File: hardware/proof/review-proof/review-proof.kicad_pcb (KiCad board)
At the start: 4 copper layers, 92 x 60 mm, 31 parts, among them J1 MAINS, J2 5V_IN, J4 LOAD, U1 VO3526, U2 AMS1117-3.3, U3 MCP6001-OT, U4 ATtiny85-20M, Y1 8MHz

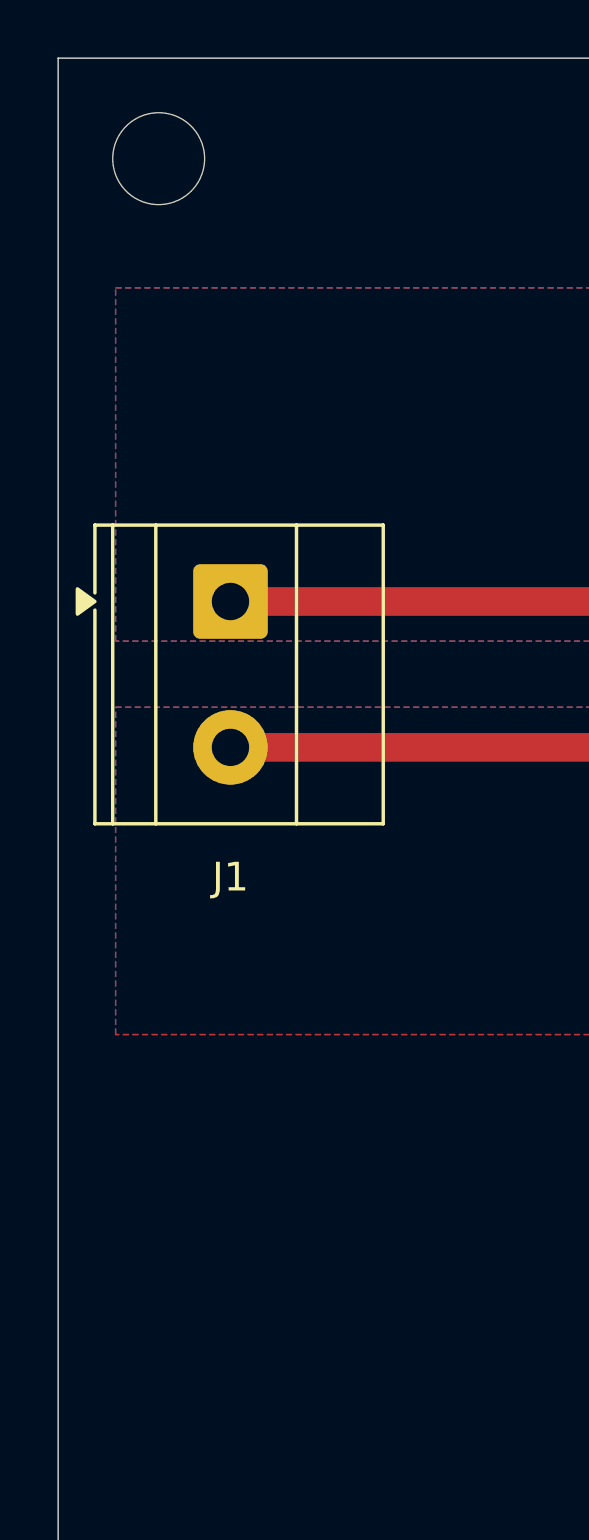
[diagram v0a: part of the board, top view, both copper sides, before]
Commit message: fix(hardware): move the review proof's mounting hole H1 clear of the mains copper the hole rule measures [SOL-PRE-ORDER-CHECK-SEPARATION-FLOOR-AND-MOUNTING-HOLES.C6]
Co-Authored-By: Claude Sonnet 5.5 <noreply@anthropic.com>
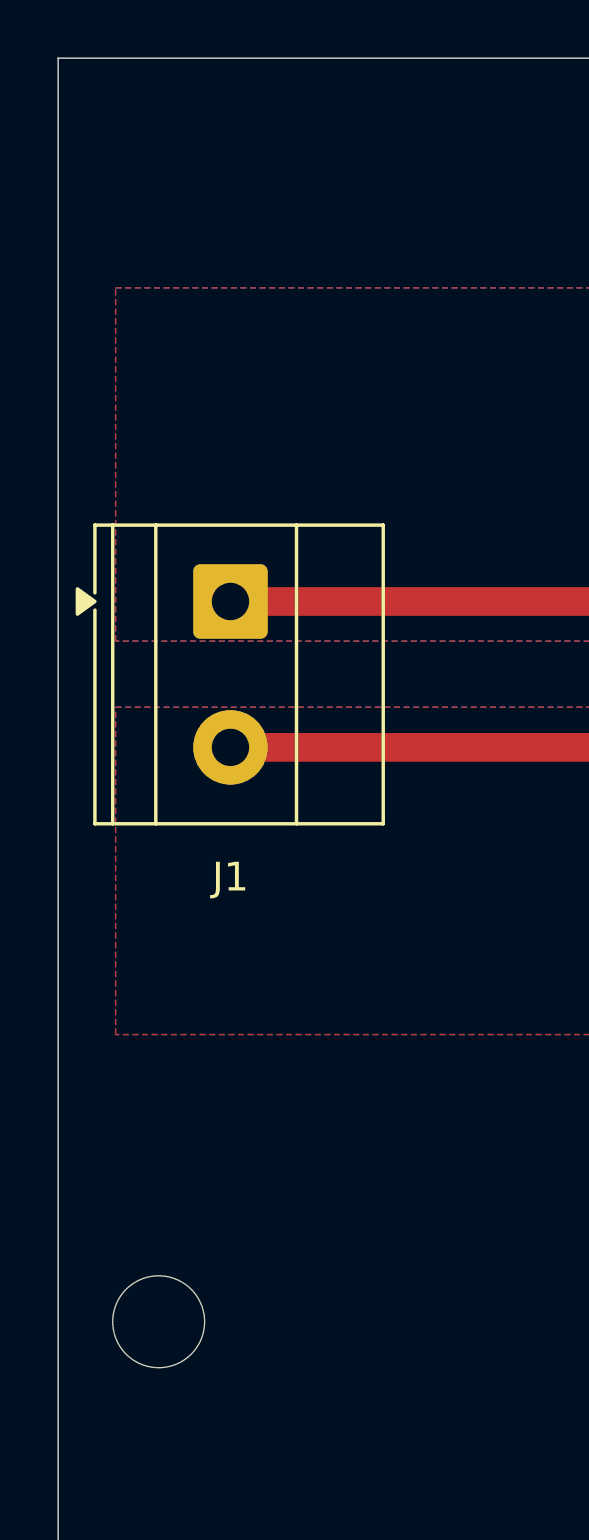
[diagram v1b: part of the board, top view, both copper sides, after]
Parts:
- moved H1 40.5 mm to (3.50, 44.0)
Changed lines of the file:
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@@
 	(footprint "MountingHole:MountingHole_3.2mm_M3"
 		(layer "F.Cu")
-		(at 3.5 3.5)
+		(at 3.5 44)
 		(descr "Mounting Hole 3.2mm, M3, no annular, generated by kicad-footprint-generator mountinghole.py")
 		(tags "mountinghole M3")

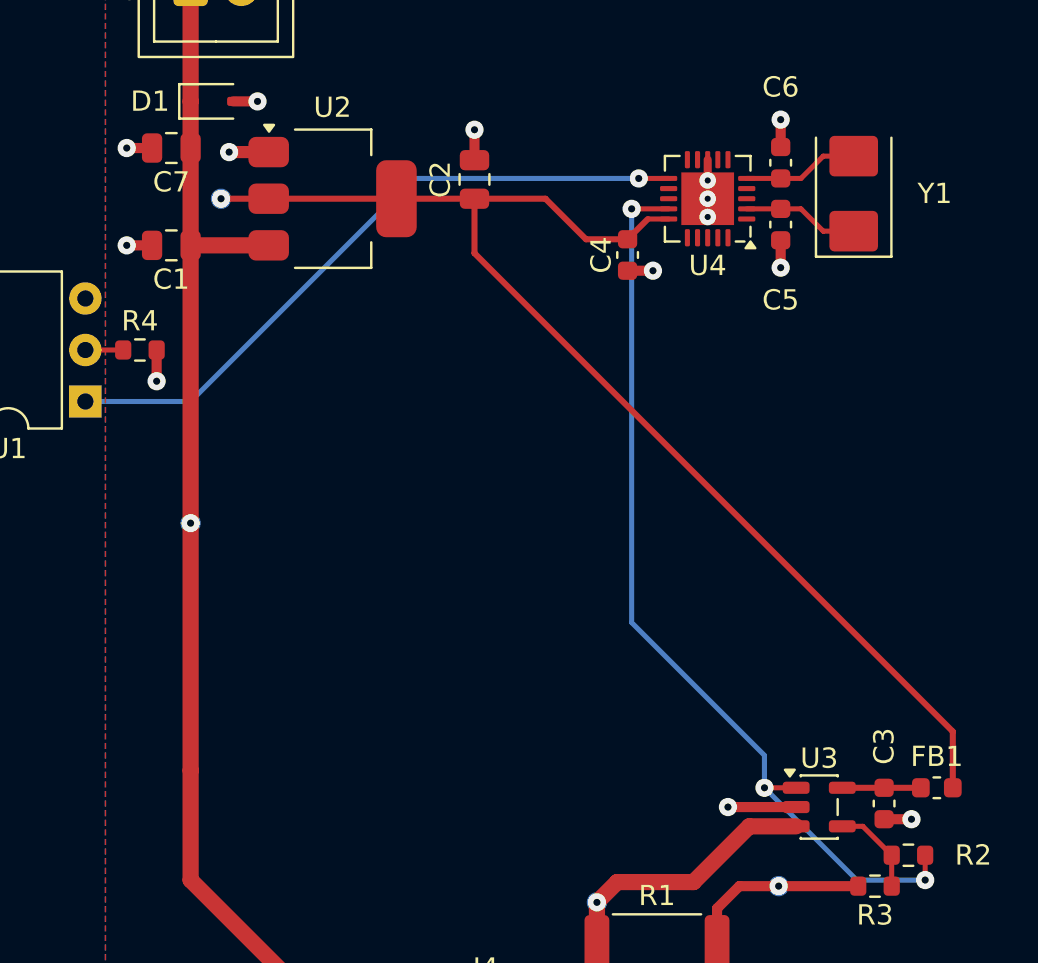
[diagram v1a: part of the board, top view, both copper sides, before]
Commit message: fix(hardware): join the review proof's decoupling and ground pins to the planes by vias beside their pads, as the amended items ask [SOL-PRE-ORDER-CHECK-SEPARATION-FLOOR-AND-MOUNTING-HOLES.C6]
Co-Authored-By: Claude Sonnet 5.5 <noreply@anthropic.com>
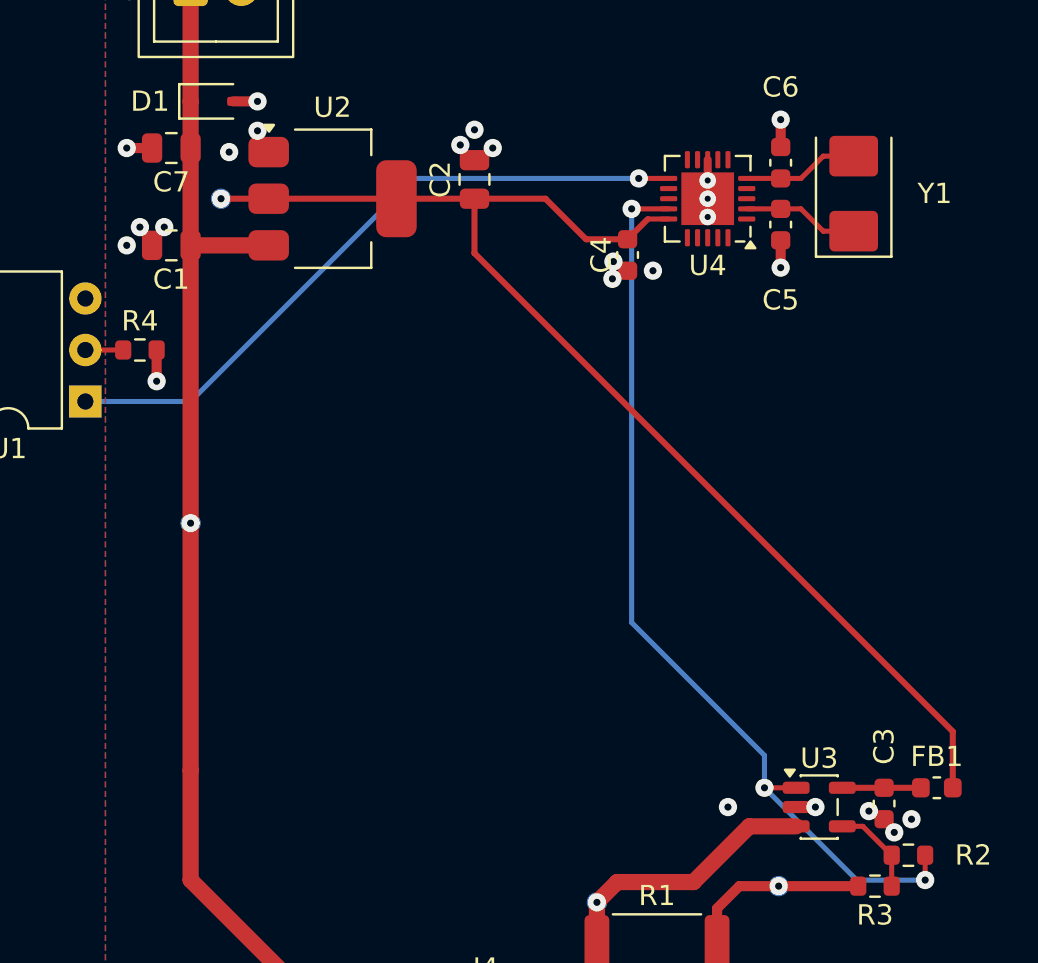
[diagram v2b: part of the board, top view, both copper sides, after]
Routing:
- net /GND: track 38.0 -> 27.3 mm, vias 21 -> 31
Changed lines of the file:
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@@
-	)
-	(segment
-		(start 51 12.1)
-		(end 51 10.6)
-		(width 0.5)
-		(layer "F.Cu")
-		(net "/GND")
-	)
-	(segment
-		(start 35.1 16.3)
-		(end 33.85 16.3)
-		(width 0.5)
-		(layer "F.Cu")
-		(net "/GND")
 	)
 	(segment
@@
 	)
 	(segment
-		(start 71.2 44.6)
-		(end 72.55 44.6)
-		(width 0.5)
-		(layer "F.Cu")
-		(net "/GND")
-	)
-	(segment
 		(start 66.1 11.45)
 		(end 66.1 10.1)
@@
 	)
 	(segment
-		(start 58.55 17.55)
-		(end 59.8 17.55)
-		(width 0.5)
-		(layer "F.Cu")
-		(net "/GND")
-	)
-	(segment
-		(start 66.8625 44)
-		(end 63.5 44)
-		(width 0.5)
-		(layer "F.Cu")
-		(net "/GND")
-	)
-	(segment
 		(start 46 57.4)
 		(end 46 58.9)
@@
 		(end 62.962 56.4)
 		(width 0.5)
-		(layer "F.Cu")
-		(net "/GND")
-	)
-	(segment
-		(start 40.85 11.7)
-		(end 38.9 11.7)
-		(width 0.6)
 		(layer "F.Cu")
 		(net "/GND")
@@
 	)
 	(via
+		(at 35.7 15.4)
+		(size 0.9)
+		(drill 0.35)
+		(layers "F.Cu" "B.Cu")
+		(net "/GND")
+	)
+	(via
 		(at 62.962 55.2)
 		(size 0.9)
@@
 	)
 	(via
+		(at 70.45 44.2)
+		(size 0.9)
+		(drill 0.35)
+		(layers "F.Cu" "B.Cu")
+		(net "/GND")
+	)
+	(via
 		(at 66.1 10.1)
 		(size 0.9)
@@
 	)
 	(via
+		(at 34.5 15.4)
+		(size 0.9)
+		(drill 0.35)
+		(layers "F.Cu" "B.Cu")
+		(net "/GND")
+	)
+	(via
 		(at 62.962 56.4)
 		(size 0.9)
@@
 	)
 	(via
+		(at 67.812 44)
+		(size 0.9)
+		(drill 0.35)
+		(layers "F.Cu" "B.Cu")
+		(net "/GND")
+	)
+	(via
+		(at 40.3 10.65)
+		(size 0.9)
+		(drill 0.35)
+		(layers "F.Cu" "B.Cu")
+		(net "/GND")
+	)
+	(via
 		(at 59.8 17.55)
 		(size 0.9)
@@
 	)
 	(via
+		(at 50.3 11.35)
+		(size 0.9)
+		(drill 0.35)
+		(layers "F.Cu" "B.Cu")
+		(net "/GND")
+	)
+	(via
 		(at 33.85 16.3)
+		(size 0.9)
+		(drill 0.35)
+		(layers "F.Cu" "B.Cu")
+		(net "/GND")
+	)
+	(via
+		(at 71.7 45.25)
+		(size 0.9)
+		(drill 0.35)
+		(layers "F.Cu" "B.Cu")
+		(net "/GND")
+	)
+	(via
+		(at 57.85 17.1)
 		(size 0.9)
 		(drill 0.35)
@@
 	)
 	(via
+		(at 57.8 17.95)
+		(size 0.9)
+		(drill 0.35)
+		(layers "F.Cu" "B.Cu")
+		(net "/GND")
+	)
+	(via
 		(at 62.962 57.6)
 		(size 0.9)
@@
 		(size 0.9)
 		(drill 0.35)
+		(layers "F.Cu" "B.Cu")
+		(net "/GND")
+	)
+	(via
+		(at 51.9 11.5)
+		(size 0.9)
+		(drill 0.35)

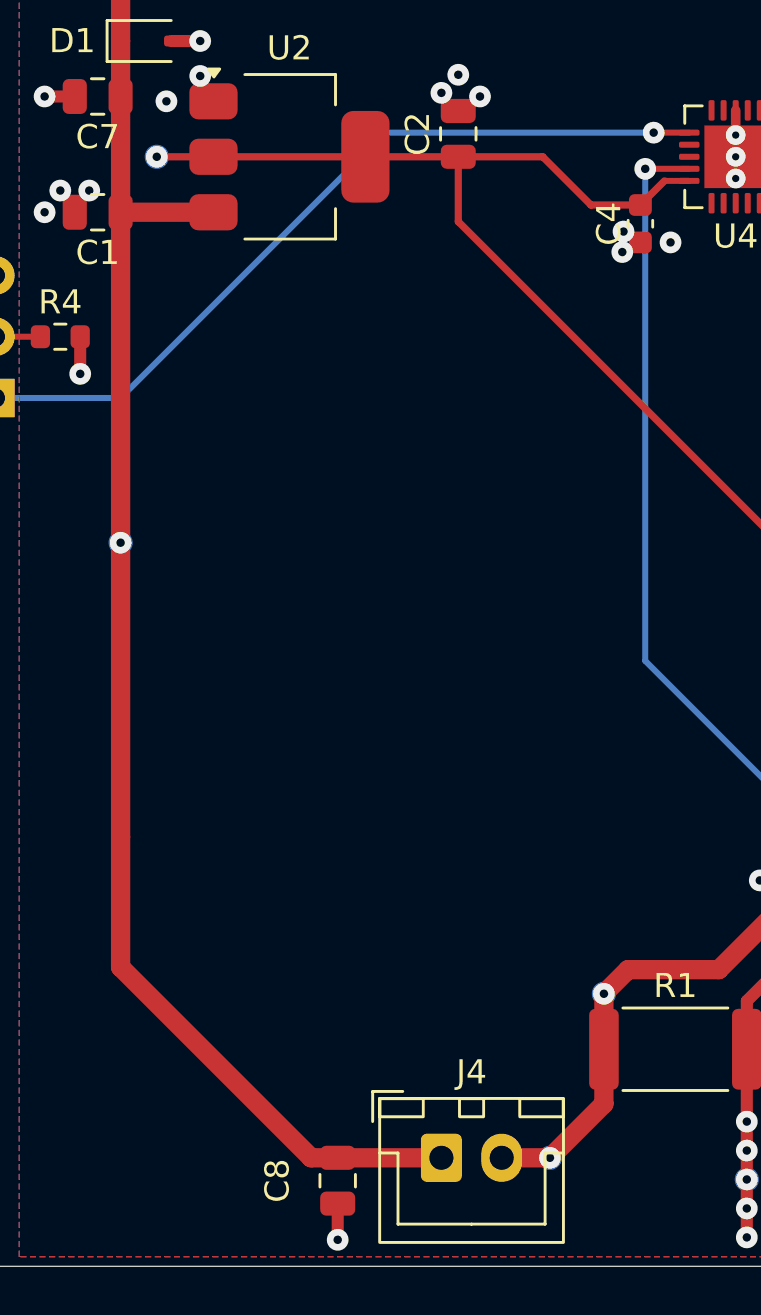
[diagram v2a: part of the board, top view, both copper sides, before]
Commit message: fix(hardware): move the review proof's test points TP2, TP3 and TP4 clear of part courtyards and state why AMP_OUT's feedback leg changes layer [SOL-PRE-ORDER-CHECK-SEPARATION-FLOOR-AND-MOUNTING-HOLES.C6]
Co-Authored-By: Claude Sonnet 5.5 <noreply@anthropic.com>
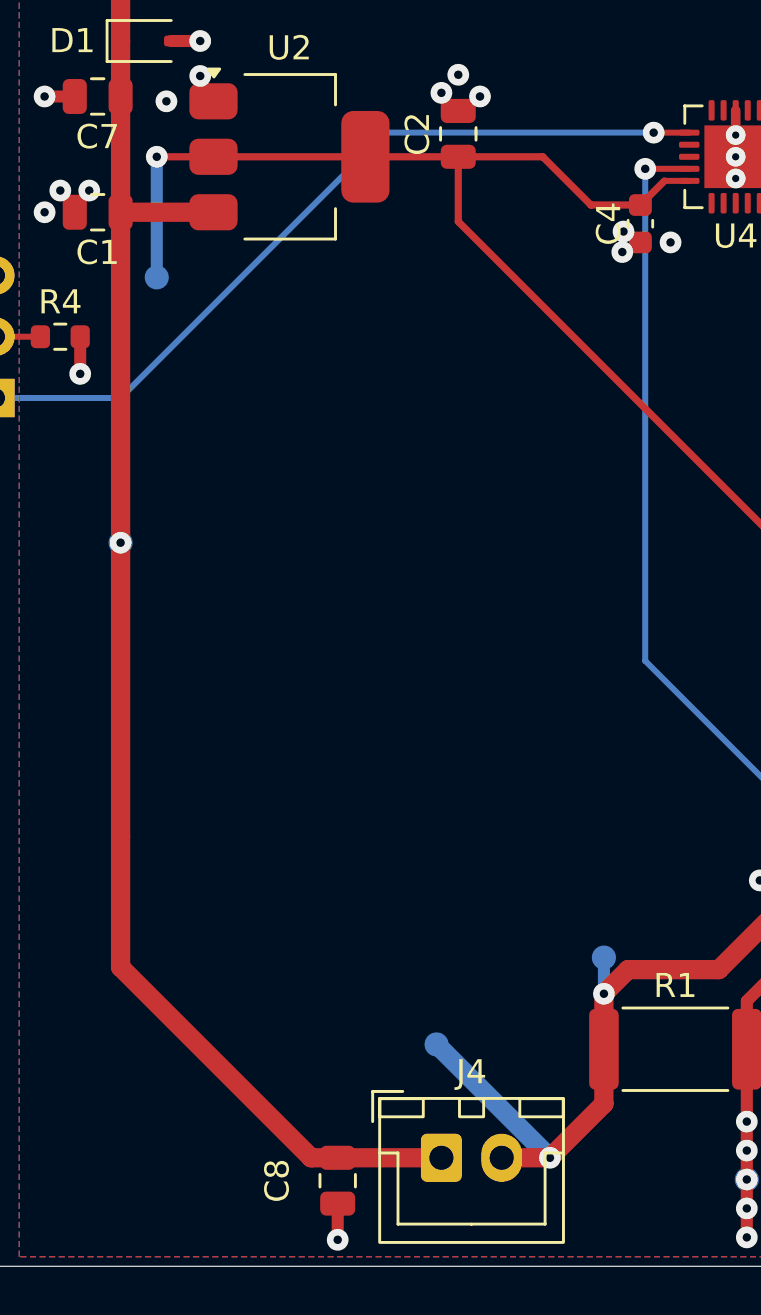
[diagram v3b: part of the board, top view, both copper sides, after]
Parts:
- moved TP3 6.65 mm to (50.1, 50.8)
- moved TP2 5.00 mm to (38.5, 19.0)
- moved TP4 1.50 mm to (57.0, 47.2)
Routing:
- net /LOAD_RTN: track 21.1 -> 29.3 mm
- net /+3V3: track 62.1 -> 67.1 mm
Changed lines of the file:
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@@
 	(footprint "TestPoint:TestPoint_Pad_D1.0mm"
 		(layer "B.Cu")
-		(at 38.5 14)
+		(at 38.5 19)
 		(descr "SMD pad as test Point, diameter 1.0mm")
 		(tags "test point SMD pad")
@@
 	(footprint "TestPoint:TestPoint_Pad_D1.0mm"
 		(layer "B.Cu")
-		(at 54.8 55.5)
+		(at 50.1 50.8)
 		(descr "SMD pad as test Point, diameter 1.0mm")
 		(tags "test point SMD pad")
@@
 	(footprint "TestPoint:TestPoint_Pad_D1.0mm"
 		(layer "B.Cu")
-		(at 57.0375 48.7)
+		(at 57.0375 47.2)
 		(descr "SMD pad as test Point, diameter 1.0mm")
 		(tags "test point SMD pad")
@@
 	)
 	(segment
+		(start 38.5 14)
+		(end 38.5 19)
+		(width 0.5)
+		(layer "B.Cu")
+		(net "/+3V3")
+	)
+	(segment
 		(start 37 30)
 		(end 37 42.2)
@@
 		(net "/LOAD_RTN")
 	)
+	(segment
+		(start 54.8 55.5)
+		(end 50.1 50.8)
+		(width 0.8)
+		(layer "B.Cu")
+		(net "/LOAD_RTN")
+	)
+	(segment
+		(start 57.0375 48.7)
+		(end 57.0375 47.2)
+		(width 0.5)
+		(layer "B.Cu")
+		(net "/LOAD_RTN")
+	)

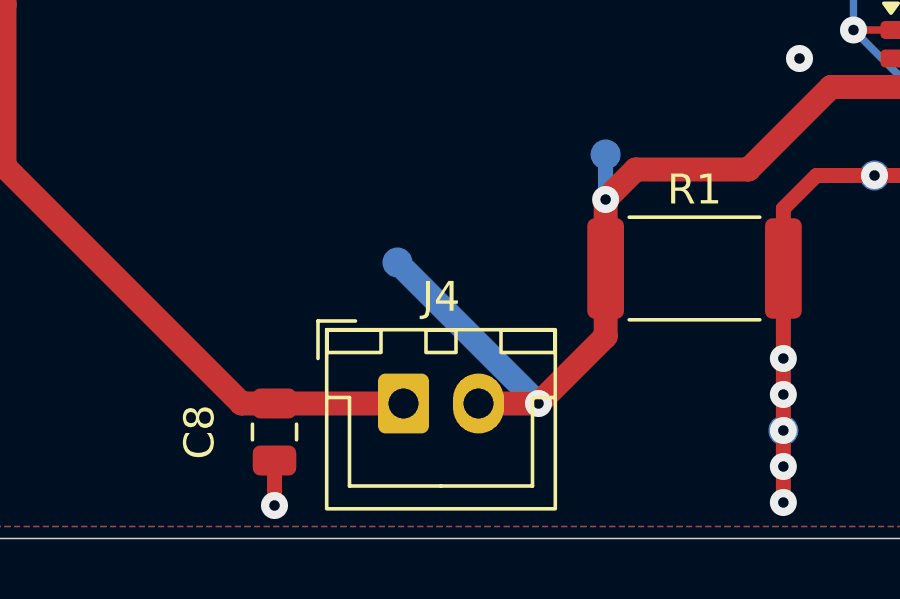
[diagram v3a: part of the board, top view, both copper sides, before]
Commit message: fix(hardware): hold test point TP3 2.0 mm from the tall connector J4, as the test point item asks [SOL-PRE-ORDER-CHECK-SEPARATION-FLOOR-AND-MOUNTING-HOLES.C6]
Co-Authored-By: Claude Sonnet 5.5 <noreply@anthropic.com>
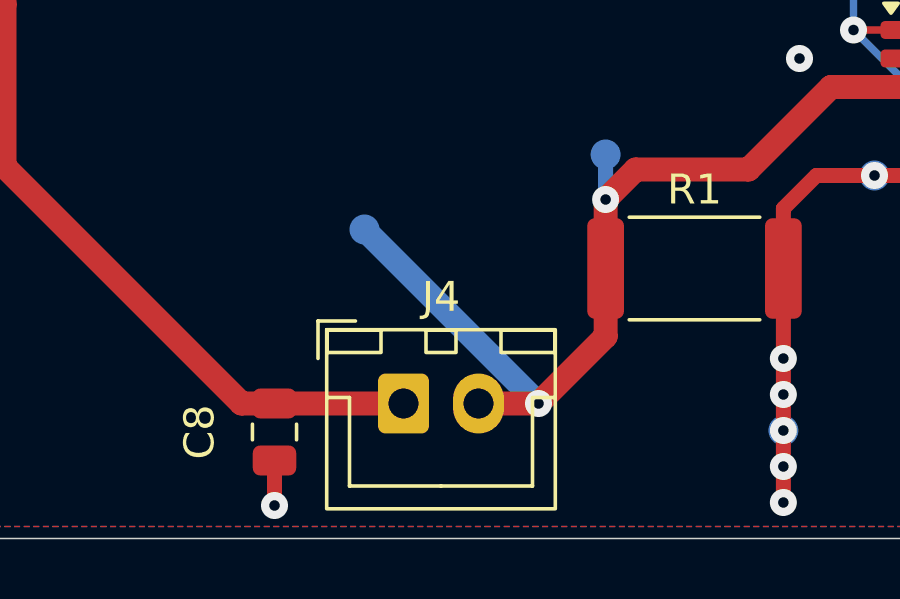
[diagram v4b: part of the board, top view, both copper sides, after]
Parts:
- moved TP3 1.56 mm to (49.0, 49.7)
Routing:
- net /LOAD_RTN: track 29.3 -> 30.8 mm
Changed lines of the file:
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@@
 	(footprint "TestPoint:TestPoint_Pad_D1.0mm"
 		(layer "B.Cu")
-		(at 50.1 50.8)
+		(at 49 49.7)
 		(descr "SMD pad as test Point, diameter 1.0mm")
 		(tags "test point SMD pad")
@@
 	)
 	(segment
-		(start 54.8 55.5)
-		(end 50.1 50.8)
-		(width 0.8)
-		(layer "B.Cu")
-		(net "/LOAD_RTN")
-	)
-	(segment
 		(start 57.0375 48.7)
 		(end 57.0375 47.2)
@@
 		(layer "B.Cu")
 		(net "/LOAD_RTN")
+	)
+	(segment
+		(start 54.8 55.5)
+		(end 49 49.7)
+		(width 0.8)
+		(layer "B.Cu")
+		(net "/LOAD_RTN")

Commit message: fix(hardware): give the tracked proof designs the three fiducials a side with surface-mount parts needs [SOL-PRE-ORDER-CHECK-FIDUCIALS-AND-POLARITY-MARKS.C5]
Co-Authored-By: Claude Sonnet 5.5 <noreply@anthropic.com>
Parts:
- added FID1: Fiducial, Fiducial:Fiducial_1mm_Mask2mm, F.Cu at (32.0, 41.0)
- added FID2: Fiducial, Fiducial:Fiducial_1mm_Mask2mm, F.Cu at (87.0, 44.0)
- added FID3: Fiducial, Fiducial:Fiducial_1mm_Mask2mm, F.Cu at (30.0, 10.0)
